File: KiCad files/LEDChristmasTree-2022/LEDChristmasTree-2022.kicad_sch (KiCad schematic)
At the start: 24 parts, among them SW1 SW_SPDT

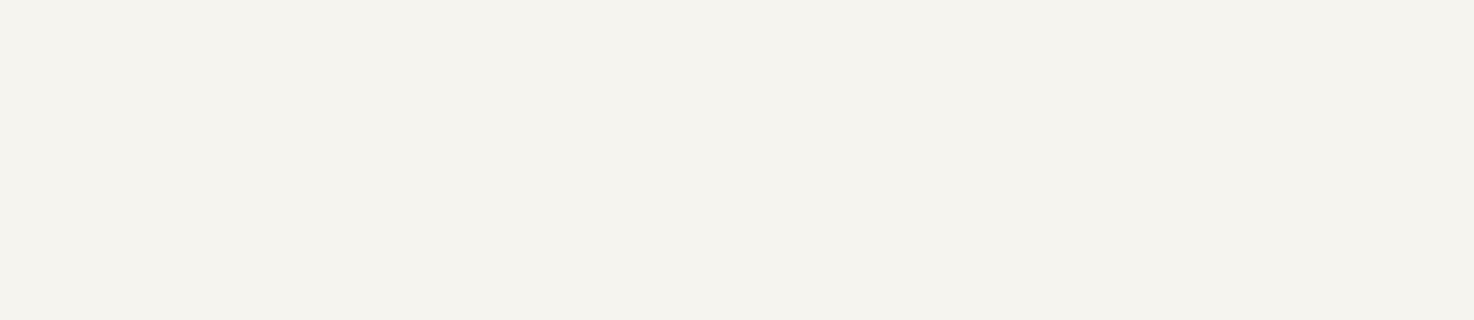
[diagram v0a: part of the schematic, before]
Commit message: Update LEDChristmasTree-2022.kicad_sch
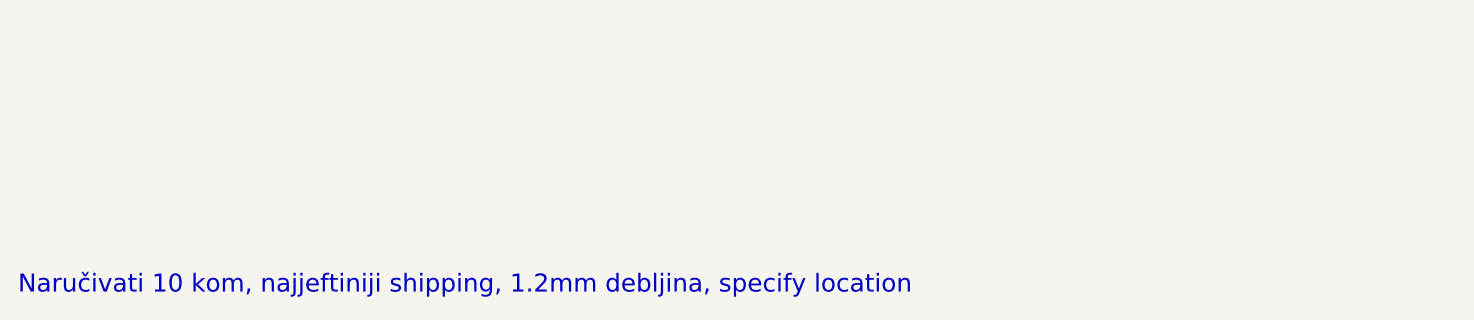
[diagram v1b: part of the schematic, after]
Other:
- note added: "Naručivati 10 kom, najjeftiniji shipping, 1.2mm debljina, specify location"
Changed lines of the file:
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@@
     (stroke (width 0) (type default) (color 0 0 0 0))
+  )
+  (text "Naručivati 10 kom, najjeftiniji shipping, 1.2mm debljina, specify location"
+    (at 56.515 135.89 0)
+    (effects (font (size 2 2)) (justify left bottom))
   )
   (symbol (lib_id "Device:LED_Small") (at 111.76 81.28 270) (unit 1)

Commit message: layout
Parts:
- added D12: RGB, Library:LED-0807, symbol Device:LED_Small
- added R12: 2k, Resistor_SMD:R_0603_1608Metric, symbol Device:R_Small
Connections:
- net GND: now also D12.2 (A)
- net at R1.1, R10.1, R11.1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: now also R12.1
- new net: D12.1 (K), R12.2
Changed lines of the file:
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@@
   (junction (at 190.5 65.405) (diameter 0) (color 0 0 0 0)
   )
+  (junction (at 254 65.405) (diameter 0) (color 0 0 0 0)
+  )
   (junction (at 142.24 65.405) (diameter 0) (color 0 0 0 0)
   )
@@
   )
   (junction (at 203.2 65.405) (diameter 0) (color 0 0 0 0)
+  )
+  (junction (at 254 89.535) (diameter 0) (color 0 0 0 0)
   )
   (junction (at 241.3 89.535) (diameter 0) (color 0 0 0 0)
@@
     (stroke (width 0) (type default) (color 0 0 0 0))
   )
+  (wire (pts (xy 266.7 74.295) (xy 266.7 78.74))
+    (stroke (width 0) (type default) (color 0 0 0 0))
+  )
   (wire (pts (xy 190.5 65.405) (xy 203.2 65.405))
     (stroke (width 0) (type default) (color 0 0 0 0))
@@
     (stroke (width 0) (type default) (color 0 0 0 0))
   )
+  (wire (pts (xy 266.7 69.215) (xy 266.7 65.405))
+    (stroke (width 0) (type default) (color 0 0 0 0))
+  )
   (wire (pts (xy 142.24 89.535) (xy 163.195 89.535))
     (stroke (width 0) (type default) (color 0 0 0 0))
@@
     (stroke (width 0) (type default) (color 0 0 0 0))
   )
+  (wire (pts (xy 266.7 83.82) (xy 266.7 89.535))
+    (stroke (width 0) (type default) (color 0 0 0 0))
+  )
   (wire (pts (xy 241.3 83.82) (xy 241.3 89.535))
     (stroke (width 0) (type default) (color 0 0 0 0))
@@
     (stroke (width 0) (type default) (color 0 0 0 0))
   )
+  (wire (pts (xy 254 89.535) (xy 266.7 89.535))
+    (stroke (width 0) (type default) (color 0 0 0 0))
+  )
   (wire (pts (xy 163.195 69.215) (xy 163.195 65.405))
+    (stroke (width 0) (type default) (color 0 0 0 0))
+  )
+  (wire (pts (xy 254 65.405) (xy 266.7 65.405))
     (stroke (width 0) (type default) (color 0 0 0 0))
   )
@@
     (pin "2")
   )
+  (symbol (lib_id "Device:LED_Small") (at 266.7 81.28 270) (unit 1)
+    (in_bom yes) (on_board yes)
+    (property "Reference" "D12" (id 0) (at 269.1892 80.1116 90)
+      (effects (font (size 1.27 1.27)) (justify left))
+    )
+    (property "Value" "RGB" (id 1) (at 269.1892 82.423 90)
+      (effects (font (size 1.27 1.27)) (justify left))
+    )
+    (property "Footprint" "Library:LED-0807" (id 2) (at 266.7 81.28 90)
+      (effects (font (size 1.27 1.27)) hide)
+    )
+    (property "Datasheet" "~" (id 3) (at 266.7 81.28 90)
+      (effects (font (size 1.27 1.27)) hide)
+    )
+    (pin "1")
+    (pin "2")
+  )
   (symbol (lib_id "Symbols:Battery") (at 78.74 78.74 0) (unit 1)
     (in_bom yes) (on_board yes) (fields_autoplaced)
@@
     (pin "3")
   )
+  (symbol (lib_id "Device:R_Small") (at 266.7 71.755 0) (unit 1)
+    (in_bom yes) (on_board yes)
+    (property "Reference" "R12" (id 0) (at 268.1986 70.7898 0)
+      (effects (font (size 1.27 1.27)) (justify left))
+    )
+    (property "Value" "2k" (id 1) (at 266.7 72.39 90)
+      (effects (font (size 0.9906 0.9906)) (justify left))
+    )
+    (property "Footprint" "Resistor_SMD:R_0603_1608Metric" (id 2) (at 266.7 71.755 0)
+      (effects (font (size 1.27 1.27)) hide)
+    )
+    (property "Datasheet" "~" (id 3) (at 266.7 71.755 0)
+      (effects (font (size 1.27 1.27)) hide)
+    )
+    (pin "1")
+    (pin "2")
+  )
   (symbol (lib_id "Device:R_Small") (at 190.5 71.755 0) (unit 1)
     (in_bom yes) (on_board yes)
@@
       (reference "D11") (unit 1) (value "RGB") (footprint "Library:LED-0807")
     )
+    (path "/a2aa815a-8dc4-43b6-bc32-bb35c0f3d442"
+      (reference "D12") (unit 1) (value "RGB") (footprint "Library:LED-0807")
+    )
     (path "/fa1d3d41-de91-4607-87ae-3b485de979cc"
       (reference "R1") (unit 1) (value "2k") (footprint "Resistor_SMD:R_0603_1608Metric")
@@
       (reference "R11") (unit 1) (value "2k") (footprint "Resistor_SMD:R_0603_1608Metric")
     )
+    (path "/b5ea958d-0cfd-4df9-ac20-3edbdc47b6ee"
+      (reference "R12") (unit 1) (value "2k") (footprint "Resistor_SMD:R_0603_1608Metric")
+    )
     (path "/00000000-0000-0000-0000-0000616a35dd"

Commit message: layout
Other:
- note added: "Naručivati 10 kom, najjeftiniji shipping, 1.2mm debljina, specify location - logo jk - naprijed silk ukrasi"
- note removed: "Naručivati 10 kom, najjeftiniji shipping, 1.2mm debljina, specify location"
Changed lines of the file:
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@@
     (stroke (width 0) (type default) (color 0 0 0 0))
   )
-  (text "Naručivati 10 kom, najjeftiniji shipping, 1.2mm debljina, specify location"
+  (text "Naručivati 10 kom, najjeftiniji shipping, 1.2mm debljina, specify location\n\n- logo jk\n- naprijed silk ukrasi"
     (at 56.515 135.89 0)
     (effects (font (size 2 2)) (justify left bottom))

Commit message: up
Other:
- note added: "Naručivati 10 kom, najjeftiniji shipping, 1.2mm debljina, specify location - logo jk - naprijed silk ukrasi - naprijed copper ukrasi"
- note removed: "Naručivati 10 kom, najjeftiniji shipping, 1.2mm debljina, specify location - logo jk - naprijed silk ukrasi"
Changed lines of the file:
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@@
     (stroke (width 0) (type default) (color 0 0 0 0))
   )
-  (text "Naručivati 10 kom, najjeftiniji shipping, 1.2mm debljina, specify location\n\n- logo jk\n- naprijed silk ukrasi"
+  (text "Naručivati 10 kom, najjeftiniji shipping, 1.2mm debljina, specify location\n\n- logo jk\n- naprijed silk ukrasi\n- naprijed copper ukrasi"
     (at 56.515 135.89 0)
     (effects (font (size 2 2)) (justify left bottom))

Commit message: gerber
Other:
- note added: "Naručivati 10 kom, najjeftiniji shipping, 1.2mm debljina, specify location - naprijed copper ukrasi"
- note removed: "Naručivati 10 kom, najjeftiniji shipping, 1.2mm debljina, specify location - logo jk - naprijed silk ukrasi - naprijed copper ukrasi"
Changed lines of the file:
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@@
     (stroke (width 0) (type default) (color 0 0 0 0))
   )
-  (text "Naručivati 10 kom, najjeftiniji shipping, 1.2mm debljina, specify location\n\n- logo jk\n- naprijed silk ukrasi\n- naprijed copper ukrasi"
+  (text "Naručivati 10 kom, najjeftiniji shipping, 1.2mm debljina, specify location\n\n- naprijed copper ukrasi"
     (at 56.515 135.89 0)
     (effects (font (size 2 2)) (justify left bottom))

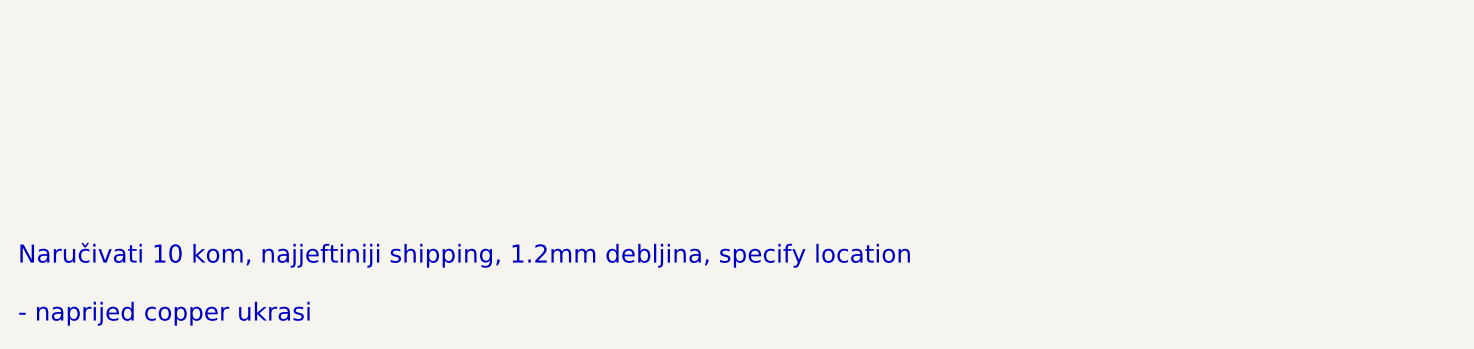
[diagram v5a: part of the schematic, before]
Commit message: Update LEDChristmasTree-2022.kicad_sch
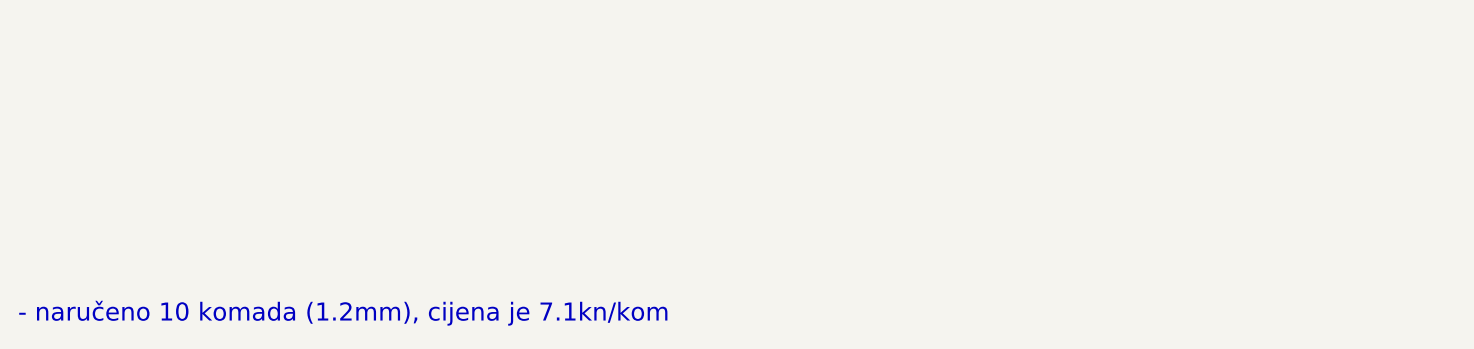
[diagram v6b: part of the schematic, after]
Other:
- note added: "- naručeno 10 komada (1.2mm), cijena je 7.1kn/kom"
- note removed: "Naručivati 10 kom, najjeftiniji shipping, 1.2mm debljina, specify location - naprijed copper ukrasi"
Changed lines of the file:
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@@
     (stroke (width 0) (type default) (color 0 0 0 0))
   )
-  (text "Naručivati 10 kom, najjeftiniji shipping, 1.2mm debljina, specify location\n\n- naprijed copper ukrasi"
-    (at 56.515 135.89 0)
+  (text "- naručeno 10 komada (1.2mm), cijena je 7.1kn/kom" (at 56.515 135.89 0)
     (effects (font (size 2 2)) (justify left bottom))
   )

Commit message: update
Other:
- note added: "- naručeno 10 komada (1.2mm) pločica, cijena je 7.1kn/kom - naručeno 21 komad 2xAAA kučišta za baterije, cijena je 6,2kn/kom TODO: - složiti da se polaritet baterija i oznake poklapaju"
- note removed: "- naručeno 10 komada (1.2mm), cijena je 7.1kn/kom"
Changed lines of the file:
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@@
     (stroke (width 0) (type default) (color 0 0 0 0))
   )
-  (text "- naručeno 10 komada (1.2mm), cijena je 7.1kn/kom" (at 56.515 135.89 0)
+  (text "- naručeno 10 komada (1.2mm) pločica, cijena je 7.1kn/kom\n- naručeno 21 komad 2xAAA kučišta za baterije, cijena je 6,2kn/kom\n\nTODO:\n- složiti da se polaritet baterija i oznake poklapaju"
+    (at 56.515 135.89 0)
     (effects (font (size 2 2)) (justify left bottom))
   )

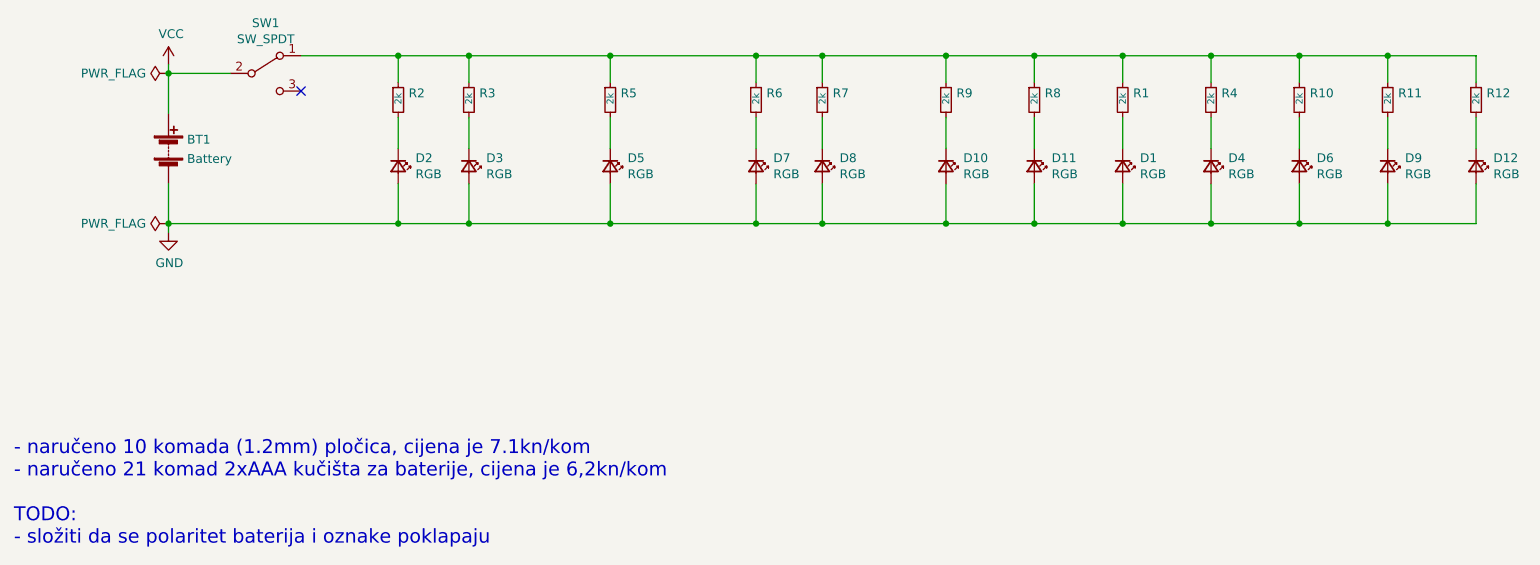
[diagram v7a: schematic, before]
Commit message: fixed battery polarity
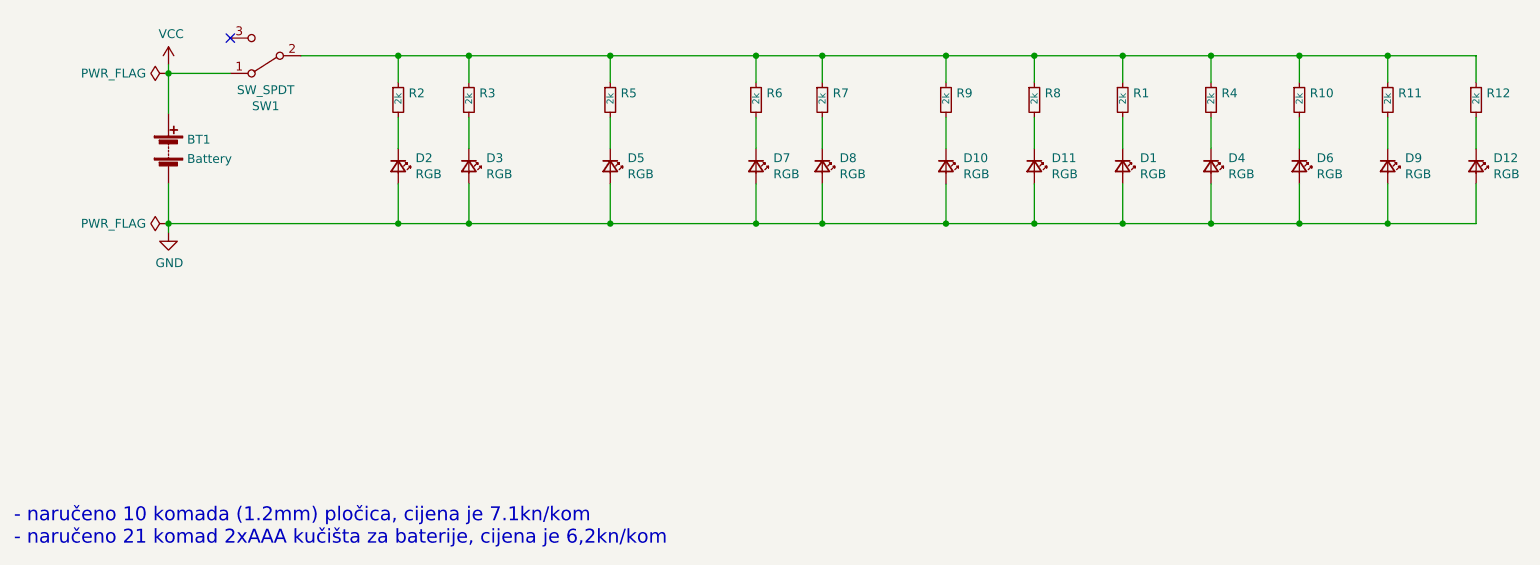
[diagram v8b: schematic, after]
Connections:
- net GND: now also BT1.1 (-); no longer BT1.3 (-)
- net VCC: now also BT1.3 (+), SW1.1 (A); no longer BT1.1 (+), SW1.2 (B)
- net at R1.1, R10.1, R11.1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: now also SW1.2 (B); no longer SW1.1 (A)
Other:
- note added: "- naručeno 10 komada (1.2mm) pločica, cijena je 7.1kn/kom - naručeno 21 komad 2xAAA kučišta za baterije, cijena je 6,2kn/kom"
- note removed: "- naručeno 10 komada (1.2mm) pločica, cijena je 7.1kn/kom - naručeno 21 komad 2xAAA kučišta za baterije, cijena je 6,2kn/kom TODO: - složiti da se polaritet baterija i oznake poklapaju"
- moved on the sheet: SW1
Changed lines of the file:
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@@
   (junction (at 163.195 65.405) (diameter 0) (color 0 0 0 0)
   )
-  (no_connect (at 97.79 70.485))
+  (no_connect (at 87.63 62.865))
   (wire (pts (xy 121.92 89.535) (xy 142.24 89.535))
     (stroke (width 0) (type default) (color 0 0 0 0))
@@
     (stroke (width 0) (type default) (color 0 0 0 0))
   )
-  (text "- naručeno 10 komada (1.2mm) pločica, cijena je 7.1kn/kom\n- naručeno 21 komad 2xAAA kučišta za baterije, cijena je 6,2kn/kom\n\nTODO:\n- složiti da se polaritet baterija i oznake poklapaju"
+  (text "- naručeno 10 komada (1.2mm) pločica, cijena je 7.1kn/kom\n- naručeno 21 komad 2xAAA kučišta za baterije, cijena je 6,2kn/kom"
     (at 56.515 135.89 0)
     (effects (font (size 2 2)) (justify left bottom))
@@
     (pin "2")
   )
-  (symbol (lib_id "Switch:SW_SPDT") (at 92.71 67.945 0) (unit 1)
-    (in_bom yes) (on_board yes)
-    (property "Reference" "SW1" (id 0) (at 92.71 60.706 0))
-    (property "Value" "SW_SPDT" (id 1) (at 92.71 63.0174 0))
-    (property "Footprint" "Button_Switch_SMD:SW_SPDT_PCM12" (id 2) (at 92.71 67.945 0)
-      (effects (font (size 1.27 1.27)) hide)
-    )
-    (property "Datasheet" "~" (id 3) (at 92.71 67.945 0)
-      (effects (font (size 1.27 1.27)) hide)
-    )
+  (symbol (lib_id "Switch:SW_SPDT") (at 92.71 65.405 180) (unit 1)
+    (in_bom yes) (on_board yes)
+    (property "Reference" "SW1" (id 0) (at 92.71 72.644 0))
+    (property "Value" "SW_SPDT" (id 1) (at 92.71 70.3326 0))
+    (property "Footprint" "Button_Switch_SMD:SW_SPDT_PCM12" (id 2) (at 92.71 65.405 0)
+      (effects (font (size 1.27 1.27)) hide)
+    )
+    (property "Datasheet" "~" (id 3) (at 92.71 65.405 0)
+      (effects (font (size 1.27 1.27)) hide)
+    )
